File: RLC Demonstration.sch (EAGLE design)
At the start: 21 parts, among them J1 POWER_JACKSLT

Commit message: Update schematic
Remove extra circuits from schematic and calculate values to put response times in the millisecond range.
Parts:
- removed C2: 10uF, SparkFun-Capacitors:10UF-POLAR-RADIAL-2.5MM-KIT-25V-20%
- removed F1: 72V/0.25A, SparkFun-Fuses:PPTC_PTH
- removed L1: 1000UH, Kenny-Custom:1000UH
- removed R3, R5: 10k, SparkFun-Resistors:10KOHM-HORIZ_KIT-1/4W-5%
- removed S4, S6: (no value), SparkFun-Switches:SWITCH-SPDT-PTH-11.6X4.0MM-LOCK
- added J5: (no value), SparkFun-Connectors:CONN_03LOCK
- C1: value 10uF -> 0.1uF; device SparkFun-Capacitors:10UF-POLAR-RADIAL-2.5MM-KIT-25V-20% -> SparkFun-Capacitors:0.1UF-KIT-EZ-50V-20%
- J3: device SparkFun-Connectors:CONN_02 -> SparkFun-Connectors:CONN_03LOCK
- J4: device SparkFun-Connectors:CONN_05LOCK -> SparkFun-Connectors:CONN_03LOCK
- L2: value 1000UH -> 370mH
- R4: value 10k -> 680
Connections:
- removed net CR: C1.-, J4.3, R3.2
- removed net LR: J4.5, L1.P$2, R5.2
- removed net N$10: R4.1, S5.P
- removed net N$12: L1.P$1, S6.P
- removed net N$4: F1.2, J2.1, S1.O
- removed net N$6: R2.1, S3.P
- removed net N$8: C1.+, S4.P
- removed net R: J4.1, R1.1, S2.P
- new net RC_TOP: J4.3, R2.1, S3.P
- new net RL_TOP: J5.3, R4.1, S5.P
- new net R_TOP: J3.3, R1.1, S2.P
- net GND: now also C1.2, J2.1, J4.1, J5.1, S1.O; no longer C2.-, F1.1, R3.1, R5.1, S4.O, S6.O
- net RC: now also C1.1; no longer C2.+
- net RL: now also J5.2; no longer J4.4
- net VCC: no longer J3.2, S4.S, S6.S
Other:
- note added: "Capacitor Test Points"
- note added: "Inductor Test Points"
- note added: "Resistor Test Points"
- note removed: "Signal Behavior Test Points"
- note removed: "voltage measurement jumper"
- moved on the sheet: L2, R2, R4, S3, S5

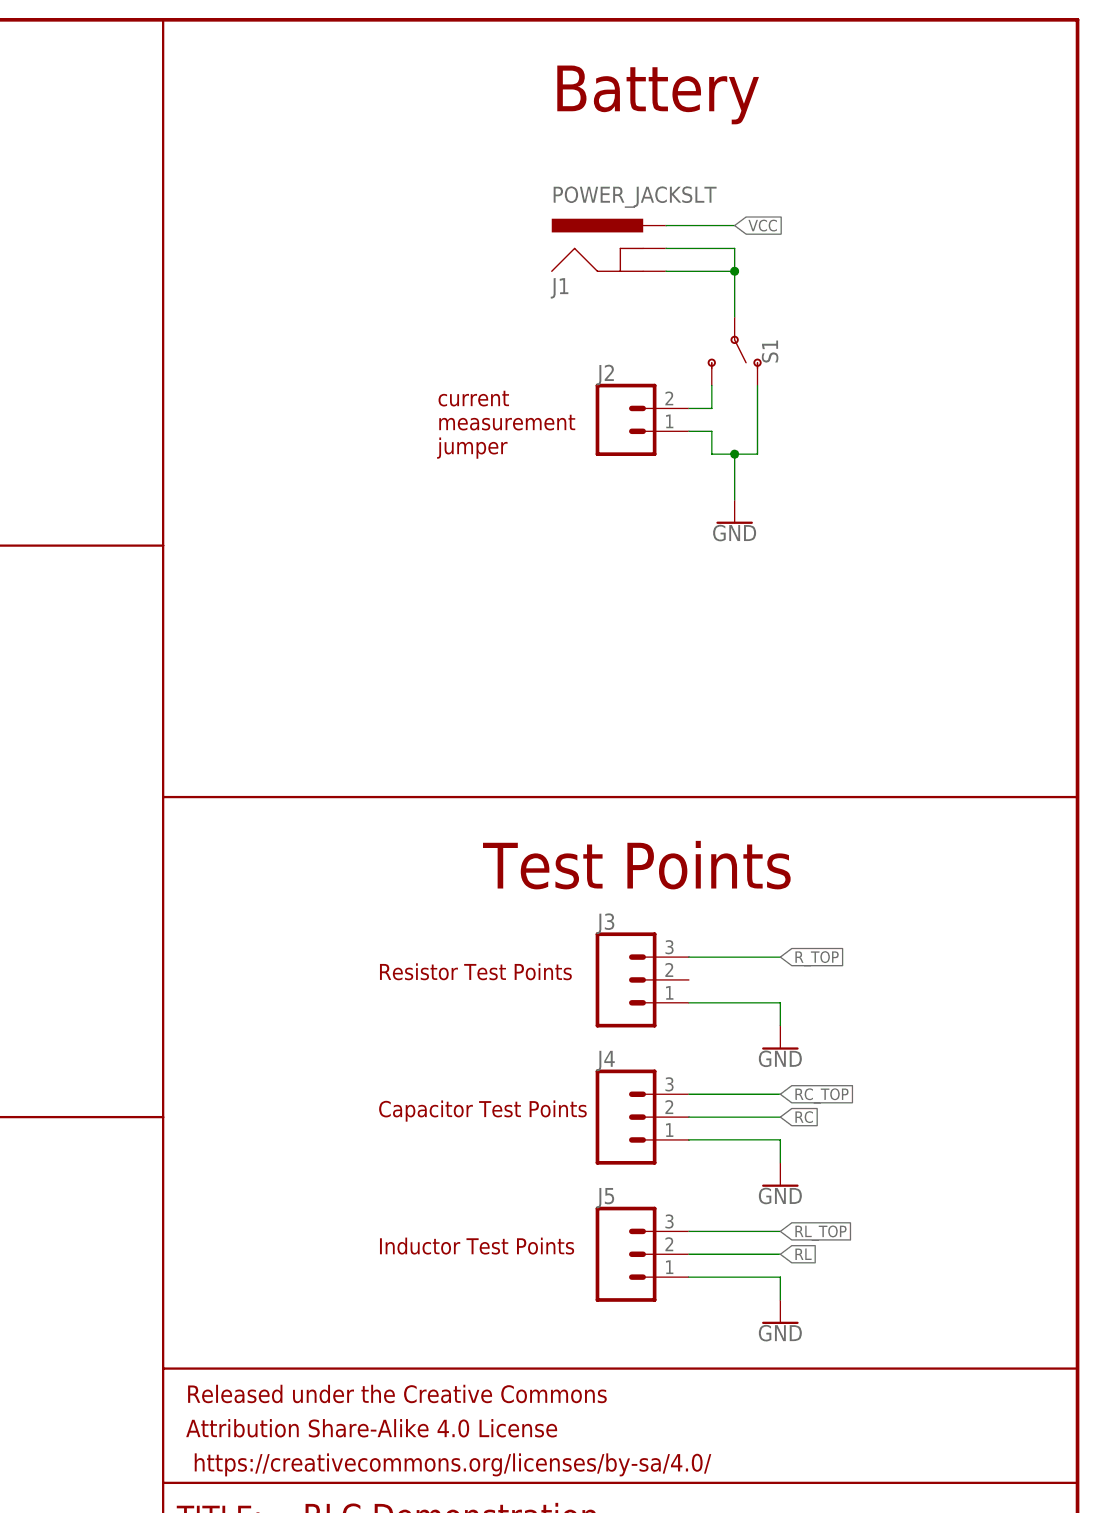
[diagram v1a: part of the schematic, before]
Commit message: Removed erroneous current measurement jumper.
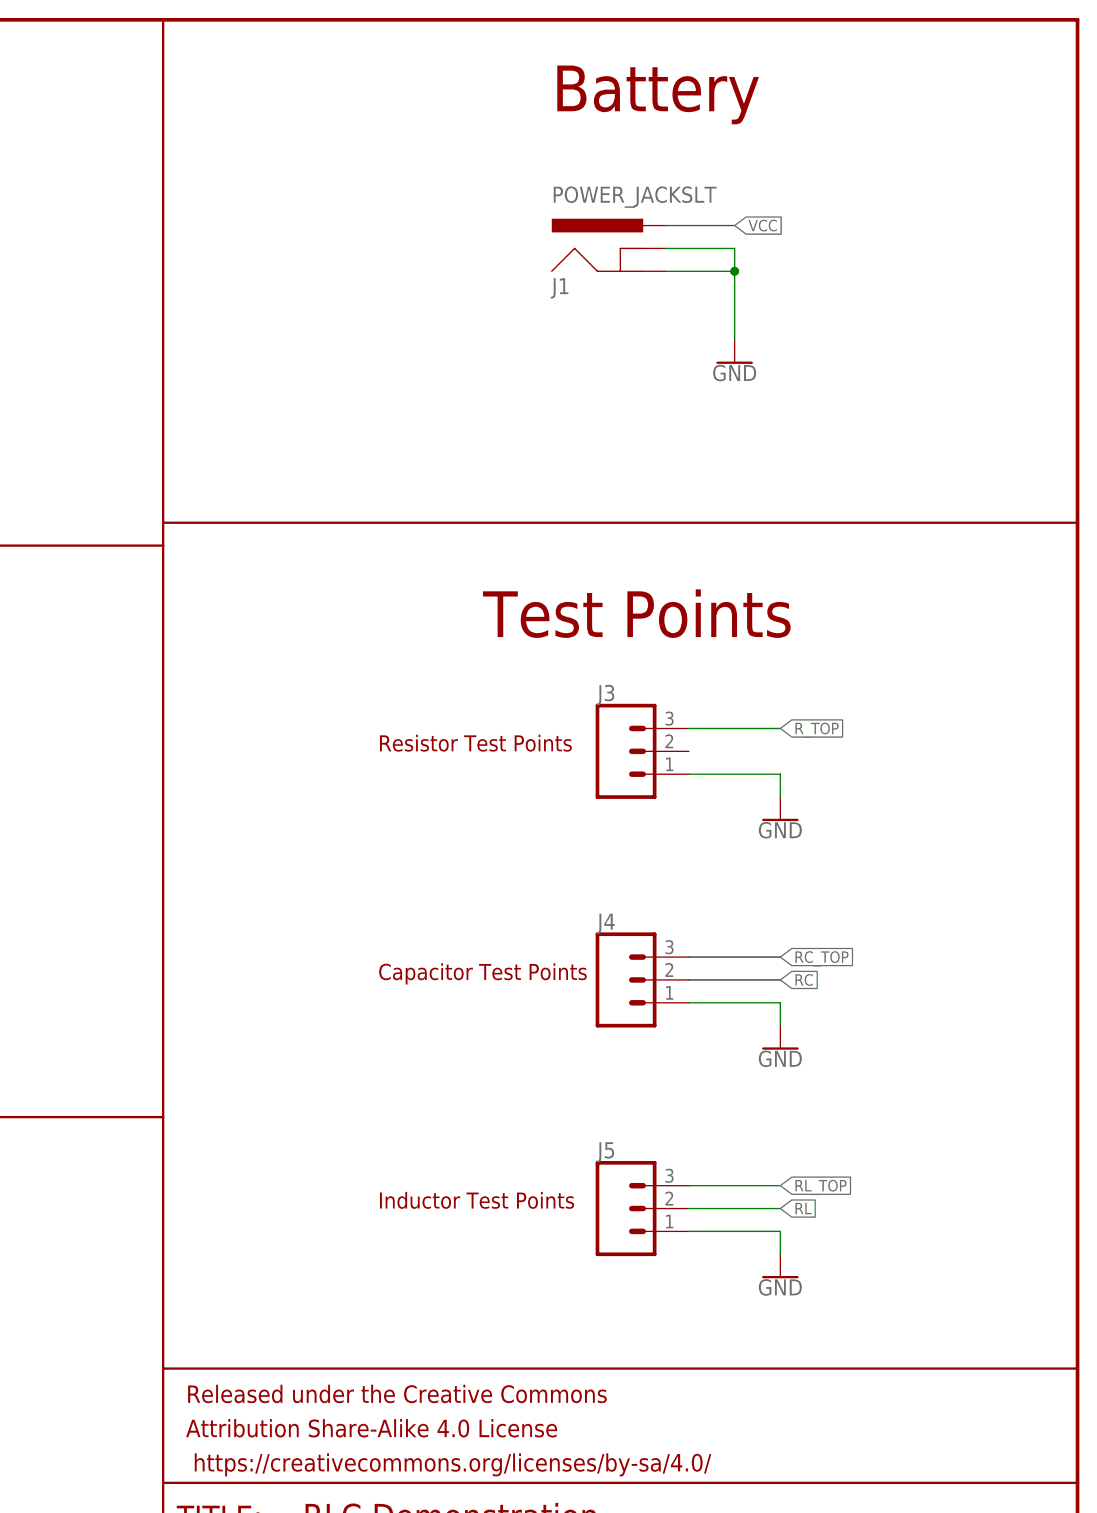
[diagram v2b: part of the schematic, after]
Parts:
- removed J2: (no value), SparkFun-Connectors:CONN_02
- removed S1: (no value), SparkFun-Switches:SWITCH-SPDT-PTH-11.6X4.0MM-LOCK
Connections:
- removed net N$2: J2.2, S1.S
- net GND: no longer J2.1, S1.O
- net N$1: no longer S1.P
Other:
- note removed: "current measurement jumper"
- moved on the sheet: J3, J4, J5

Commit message: Update Part Values
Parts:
- R4: value 680 -> 820
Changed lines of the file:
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@@
 <setting verticaltext="up"/>
 </settings>
-<grid distance="0.1" unitdist="inch" unit="inch" style="lines" multiple="1" display="yes" altdistance="0.01" altunitdist="inch" altunit="inch"/>
+<grid distance="0.1" unitdist="inch" unit="inch" style="lines" multiple="1" display="no" altdistance="0.01" altunitdist="inch" altunit="inch"/>
 <layers>
 <layer number="1" name="Top" color="4" fill="1" visible="no" active="no"/>
@@
 <part name="S3" library="SparkFun-Switches" deviceset="SWITCH-SPDT" device="-PTH-11.6X4.0MM-LOCK"/>
 <part name="GND5" library="SparkFun-PowerSymbols" deviceset="GND" device=""/>
-<part name="R4" library="SparkFun-Resistors" deviceset="10KOHM" device="-HORIZ_KIT-1/4W-5%" value="680"/>
+<part name="R4" library="SparkFun-Resistors" deviceset="10KOHM" device="-HORIZ_KIT-1/4W-5%" value="820"/>
 <part name="S5" library="SparkFun-Switches" deviceset="SWITCH-SPDT" device="-PTH-11.6X4.0MM-LOCK"/>
 <part name="J4" library="SparkFun-Connectors" deviceset="CONN_03" device="LOCK"/>

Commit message: Finalize Board Designs
Changed sch drawings to actual parts and routed board.
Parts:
- removed J5: (no value), SparkFun-Connectors:CONN_03LOCK
- removed L2: 370mH, Kenny-Custom:1000UH
- removed R4: 820, SparkFun-Resistors:10KOHM-HORIZ_KIT-1/4W-5%
- removed S5: (no value), SparkFun-Switches:SWITCH-SPDT-PTH-11.6X4.0MM-LOCK
- added J2: (no value), SparkFun-Connectors:CONN_03LOCK
- added L1: 370 mH, Kenny-Custom:KNOWLES-370MH-5100-253441
- added R3: 820, SparkFun-Resistors:10KOHM-HORIZ-1/4W-5%
- added S1: SWITCH-SPDT, Kenny-Custom:SWITCH-SPDT
- C1: value 0.1uF -> 0.1 uF; device SparkFun-Capacitors:0.1UF-KIT-EZ-50V-20% -> SamacSys_Parts:K104K15X7RF53H5
- J1: value POWER_JACKSLT -> POWER_JACKPTH_BREAD; device SparkFun-Connectors:POWER_JACKSLT -> SparkFun-Connectors:POWER_JACKPTH_BREAD
- R1, R2: device SparkFun-Resistors:10KOHM-HORIZ_KIT-1/4W-5% -> SparkFun-Resistors:10KOHM-HORIZ-1/4W-5%
- S2, S3: value (none) -> SWITCH-SPDT; device SparkFun-Switches:SWITCH-SPDT-PTH-11.6X4.0MM-LOCK -> Kenny-Custom:SWITCH-SPDT
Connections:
- removed net N$1: J1.GND, J1.GNDBREAK
- net GND: now also C1.1, J1.GND, J1.GNDBREAK, J2.1, L1.P$1, S1.P$2, S2.P$2, S3.P$2; no longer C1.2, J5.1, L2.P$2, S2.O, S3.O, S5.O
- net RC: now also C1.2, J3.2; no longer C1.1, J4.2
- net RC_TOP: now also J3.3, S1.P$1; no longer J4.3, S3.P
- net RL: now also J4.2, L1.P$2, R3.2; no longer J5.2, L2.P$1, R4.2
- net RL_TOP: now also J4.3, R3.1, S2.P$1; no longer J5.3, R4.1, S5.P
- net R_TOP: now also J2.3, S3.P$1; no longer J3.3, S2.P
- net VCC: now also S1.P$3, S2.P$3, S3.P$3; no longer S2.S, S3.S, S5.S
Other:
- moved on the sheet: J3, J4
